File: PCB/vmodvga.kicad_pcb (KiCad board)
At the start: 2 copper layers, 60 parts, among them J1 DE-15, J2 DE-15, J3 VHDCI, U1 ADP3303-3V3, U2 ADP3334, U3 AD9984, U4 ADP3334

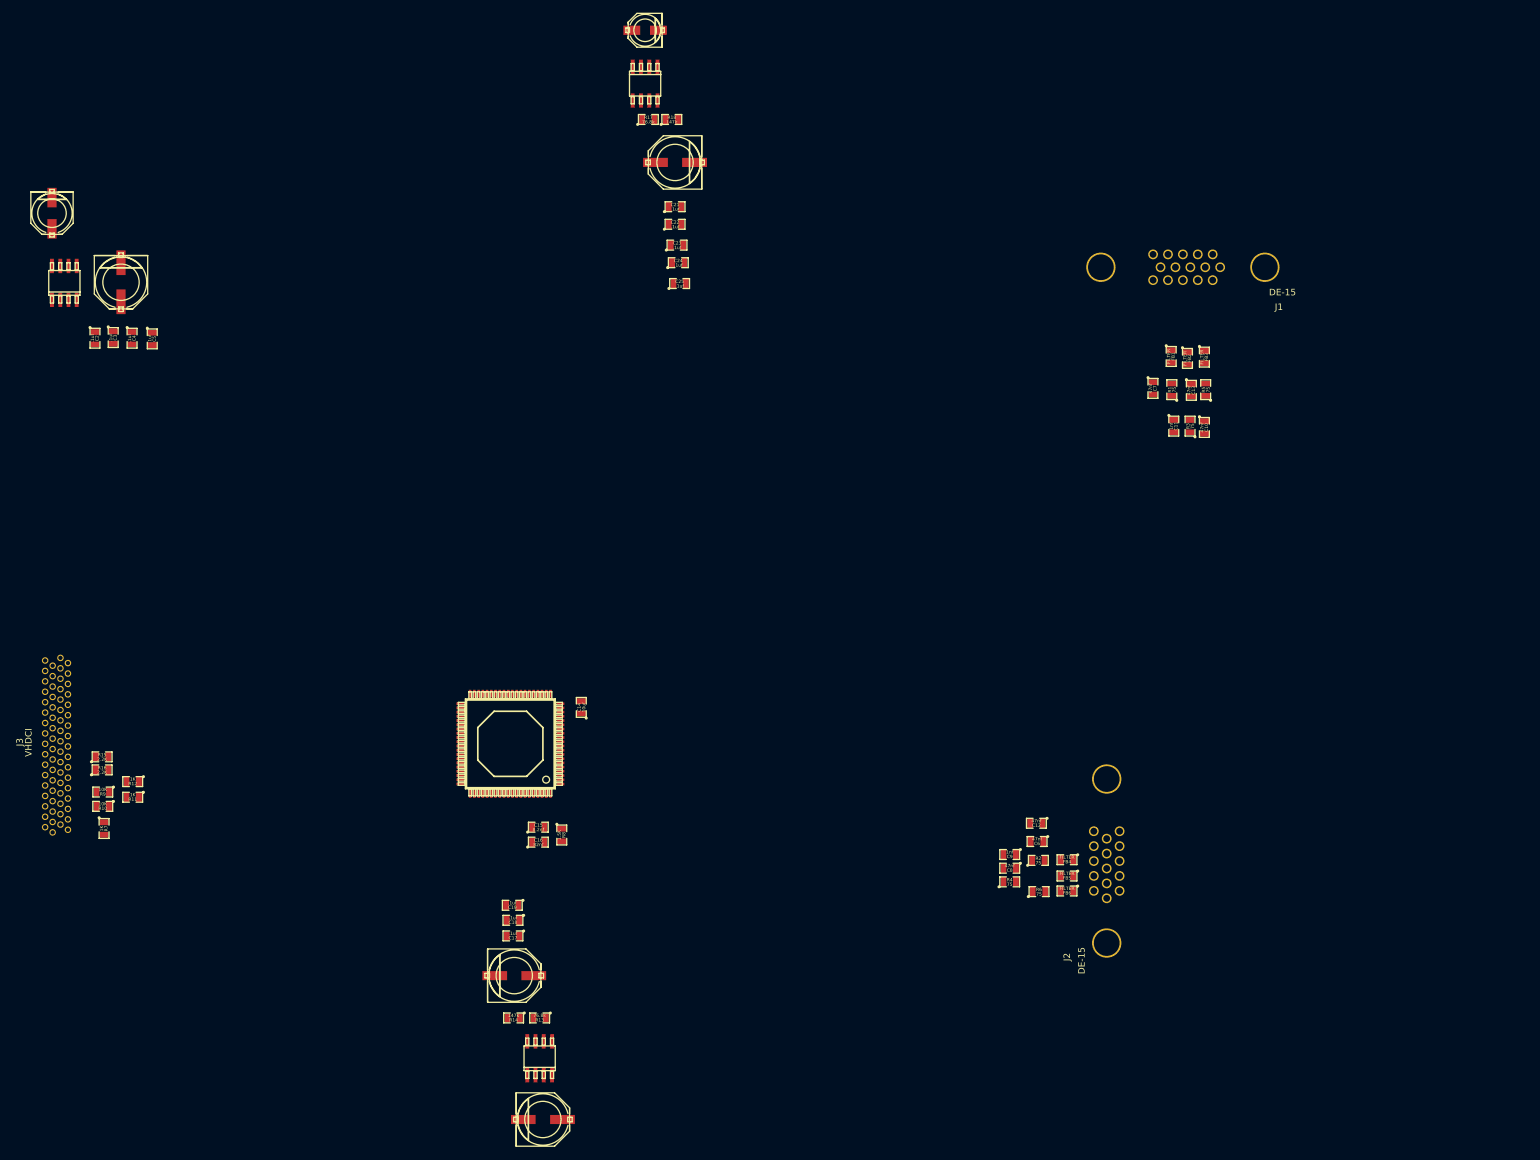
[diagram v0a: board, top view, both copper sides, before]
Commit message: Two VGA connectors without terminal resistors
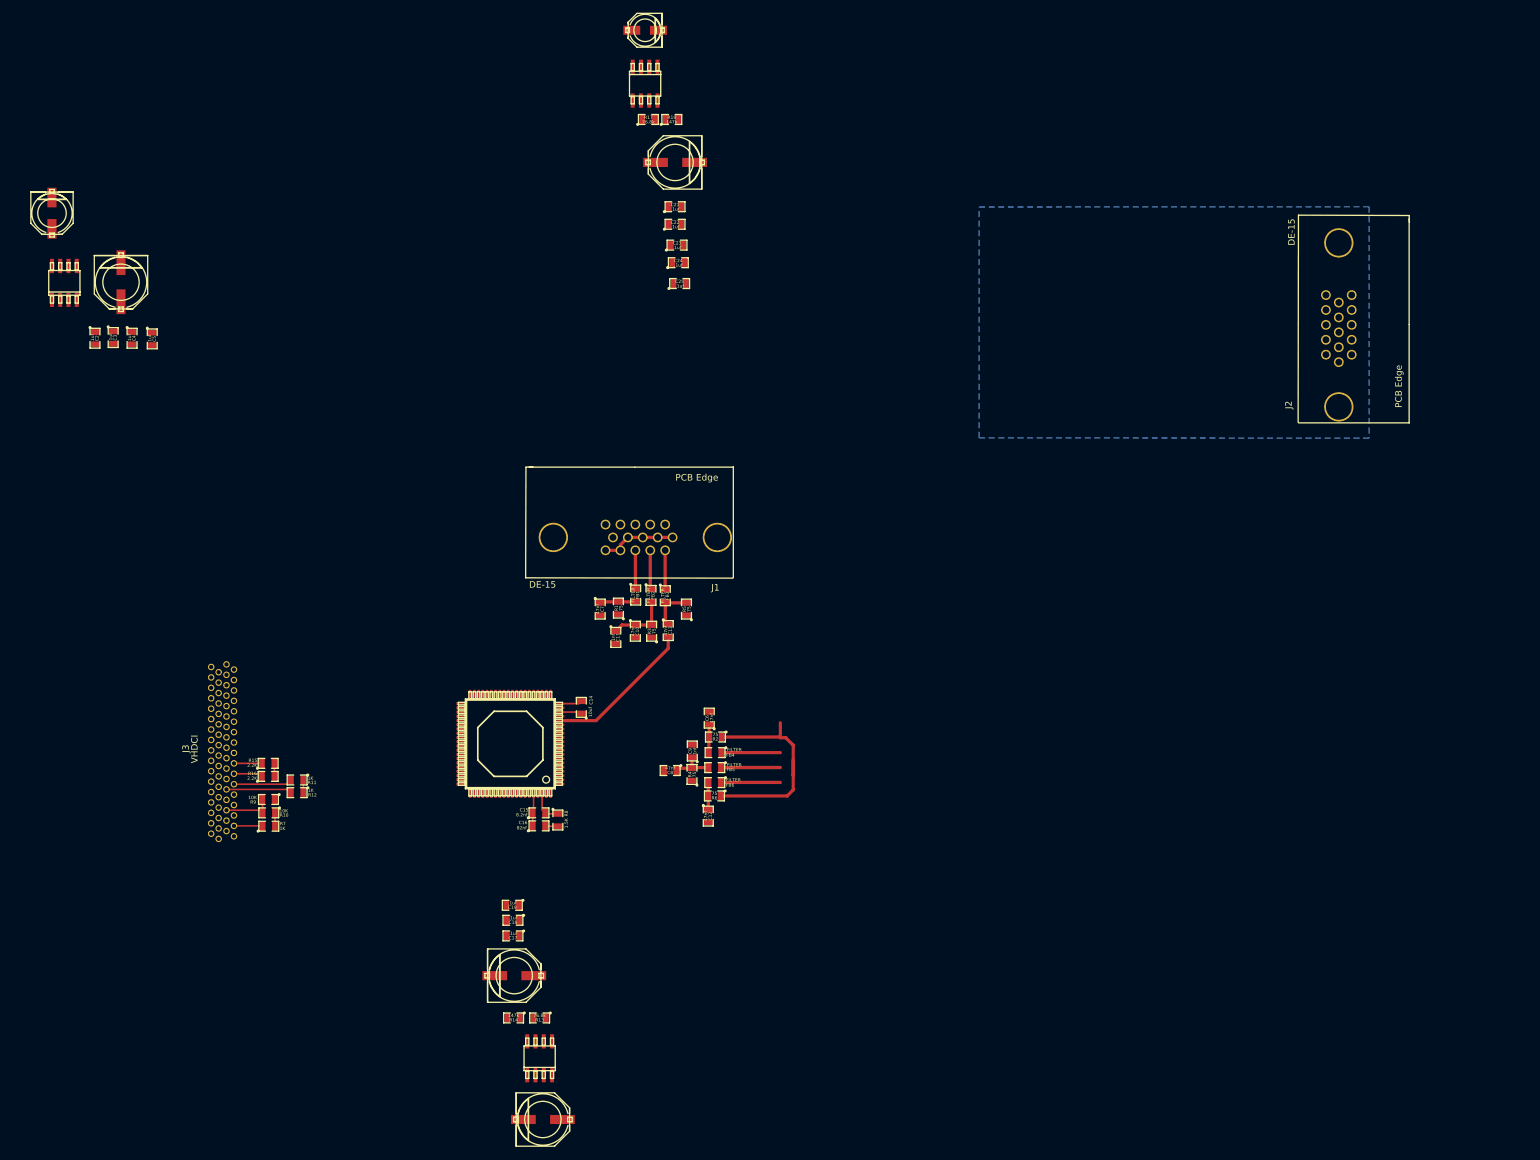
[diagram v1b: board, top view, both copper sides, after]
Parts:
- moved J1 92.9 mm to (140.1, 101.4)
- moved C10 92.8 mm to (140.1, 117.8)
- moved C11 91.6 mm to (137.1, 118.8)
- moved C7 91.4 mm to (134.7, 114.4)
- moved R1 91.4 mm to (137.5, 114.2)
- moved FB3 90.5 mm to (144.7, 112.3)
- moved J2 90.5 mm to (250.2, 70.8)
- moved FB2 90.1 mm to (142.5, 112.3)
- moved FB1 90.0 mm to (140.2, 112.2)
- moved R3 88.5 mm to (142.6, 117.8)
- moved C13 88.4 mm to (145.2, 117.7)
- moved R5 86.6 mm to (147.9, 114.4)
- moved FB5 56.6 mm to (152.3, 138.8)
- moved FB6 56.6 mm to (152.3, 141.1)
- moved FB4 56.5 mm to (152.3, 136.4)
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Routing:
- net /GND: track 0.00 -> 50.1 mm
- net N-0000012: track 0.00 -> 22.9 mm
- net /CLAMP: track 0.00 -> 10.1 mm
- net N-0000014: track 0.00 -> 9.53 mm
- net N-000005: track 0.00 -> 9.13 mm
- net N-000004: track 0.00 -> 9.12 mm
- net N-000003: track 0.00 -> 9.07 mm
- net /COST: track 0.00 -> 9.02 mm
- net /VSOUT: track 0.00 -> 7.91 mm
- net N-0000013: track 0.00 -> 6.94 mm
- net N-0000084: track 0.00 -> 6.85 mm
- net N-0000017: track 0.00 -> 6.03 mm
- net N-0000016: track 0.00 -> 6.01 mm
- net N-0000015: track 0.00 -> 5.94 mm
- net N-000009: track 0.00 -> 5.55 mm
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- added copper zone on B.Cu, net /GND
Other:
- net class Default: clearance 0.254 -> 0.125; trace_width 0.254 -> 0.25; via_dia 0.889 -> 0.45; via_drill 0.635 -> 0.3
- rule trace_clearance: 0.254 -> 0.125
- rule trace_min: 0.254 -> 0.125
- rule via_min_drill: 0.508 -> 0.3
- rule via_min_size: 0.889 -> 0.45

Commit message: Started with PCB design
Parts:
- added P1: 50R, R50x8, F.Cu at (120.3, 66.4)
- added P2: 50R, R50x8, F.Cu at (114.7, 66.6)
- added P3: 50R, R50x8, F.Cu at (108.1, 83.7)
- added P4: 50R, R50x8, F.Cu at (107.3, 77.2)
- added R19: 50, SM0805, F.Cu at (103.5, 82.7)
- added R20: 50, SM0805, F.Cu at (107.1, 81.4)
- added R21: 50, SM0805, F.Cu at (103.5, 80.1)
- added R22: 50, SM0805, F.Cu at (107.0, 78.6)
- moved Cp5 193.1 mm to (252.8, 87.0)
- moved Cp2 181.0 mm to (272.1, 86.1)
- moved C2 175.2 mm to (228.1, 111.2)
- moved U1 171.4 mm to (223.7, 69.0)
- moved C3 170.7 mm to (226.2, 111.2)
- moved R9 166.6 mm to (245.3, 103.0)
- moved C4 166.1 mm to (224.4, 111.2)
- moved R10 163.6 mm to (241.7, 103.0)
- moved Cp1 161.4 mm to (211.2, 69.3)
- moved R15 154.0 mm to (234.4, 106.5)
- moved R12 151.5 mm to (236.2, 110.3)
- moved C5 151.1 mm to (216.2, 88.8)
- moved R16 150.9 mm to (230.8, 106.5)
- moved R14 149.0 mm to (252.7, 106.7)
- moved R13 148.7 mm to (256.3, 106.7)
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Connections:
- J3 pad 1: /B1 -> (no net)
- J3 pad 10: /B7 -> (no net)
- J3 pad 12: /B8 -> (no net)
- J3 pad 13: /B9 -> (no net)
- J3 pad 20: /G0 -> (no net)
- J3 pad 22: /G1 -> (no net)
- J3 pad 23: /G2 -> (no net)
- J3 pad 25: /G3 -> (no net)
- J3 pad 26: /G4 -> (no net)
- J3 pad 28: /G5 -> (no net)
- J3 pad 29: /G6 -> (no net)
- J3 pad 3: /B2 -> (no net)
- J3 pad 31: /G7 -> (no net)
- J3 pad 32: /G8 -> (no net)
- J3 pad 34: /G9 -> (no net)
- J3 pad 35: /B0 -> (no net)
- J3 pad 37: /PWRDWN -> (no net)
- J3 pad 38: /OE_Field -> (no net)
- J3 pad 4: /B3 -> (no net)
- J3 pad 40: /VSOUT -> (no net)
- J3 pad 41: /HSOUT -> (no net)
- J3 pad 43: /SOGOUT -> (no net)
- J3 pad 44: /CLAMP -> (no net)
- J3 pad 45: /COST -> (no net)
- J3 pad 47: /SDA -> (no net)
- J3 pad 49: /SCL -> (no net)
- J3 pad 54: /R0 -> (no net)
- J3 pad 56: /R1 -> (no net)
- J3 pad 57: /R2 -> (no net)
- J3 pad 59: /R3 -> (no net)
- J3 pad 6: /B4 -> (no net)
- J3 pad 60: /R4 -> (no net)
- J3 pad 62: /R5 -> (no net)
- J3 pad 63: /R6 -> (no net)
- J3 pad 65: /R7 -> (no net)
- J3 pad 66: /R8 -> (no net)
- J3 pad 68: /R9 -> (no net)
- J3 pad 7: /B5 -> (no net)
- J3 pad 9: /B6 -> (no net)
- U3 pad 21: /OE_Field -> N-0000092
- U3 pad 22: /VSOUT -> N-0000093
- U3 pad 23: /HSOUT -> N-0000094
- U3 pad 24: /SOGOUT -> N-0000057
- U3 pad 25: /DATACK -> N-0000058
- U3 pad 28: /R9 -> N-0000059
- U3 pad 29: /R8 -> N-0000060
- U3 pad 30: /R7 -> N-0000061
- U3 pad 31: /R6 -> N-0000023
- U3 pad 32: /R5 -> N-0000022
- U3 pad 33: /R4 -> N-0000021
- U3 pad 34: /R3 -> N-0000020
- U3 pad 35: /R2 -> N-0000019
- U3 pad 36: /R1 -> N-0000018
- U3 pad 37: /R0 -> N-0000017
- U3 pad 42: /G9 -> N-0000041
- U3 pad 43: /G8 -> N-0000040
- U3 pad 44: /G7 -> N-0000039
- U3 pad 45: /G6 -> N-0000038
- U3 pad 46: /G5 -> N-0000037
- U3 pad 47: /G4 -> N-0000036
- U3 pad 48: /G3 -> N-0000035
- U3 pad 49: /G2 -> N-0000034
- U3 pad 50: /G1 -> N-0000075
- U3 pad 51: /G0 -> N-0000077
- U3 pad 54: /B9 -> N-0000073
- U3 pad 55: /B8 -> N-0000071
- U3 pad 56: /B7 -> N-0000068
- U3 pad 57: /B6 -> N-0000067
- U3 pad 58: /B5 -> N-0000066
- U3 pad 59: /B4 -> N-0000065
- U3 pad 60: /B3 -> N-0000064
- U3 pad 61: /B2 -> N-0000069
- U3 pad 62: /B1 -> N-0000062
- U3 pad 63: /B0 -> N-0000070
- U3 pad 64: /OVDD -> (no net)
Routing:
- net N-0000082: track 22.9 -> 7.19 mm
- net /CLAMP: track 10.1 -> 0.00 mm
- net /COST: track 9.02 -> 0.00 mm
- net N-0000070: track 0.00 -> 8.16 mm
- net /VSOUT: track 7.91 -> 0.00 mm
- net /GND: track 50.1 -> 58.0 mm
- net N-0000062: track 0.00 -> 7.21 mm
- net N-0000077: track 0.00 -> 7.15 mm
- net N-0000071: track 0.00 -> 7.15 mm
- net N-000007: track 0.00 -> 7.00 mm
- net N-000005: track 0.00 -> 6.98 mm
- net N-0000081: track 0.00 -> 6.77 mm
- net N-0000083: track 0.00 -> 6.75 mm
- net N-0000080: track 0.00 -> 6.57 mm
- net N-000006: track 0.00 -> 6.55 mm
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- added copper zone on F.Cu, net /GND
- removed copper zone on B.Cu, net /GND
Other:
- board outline added: 80 x 60.1 mm

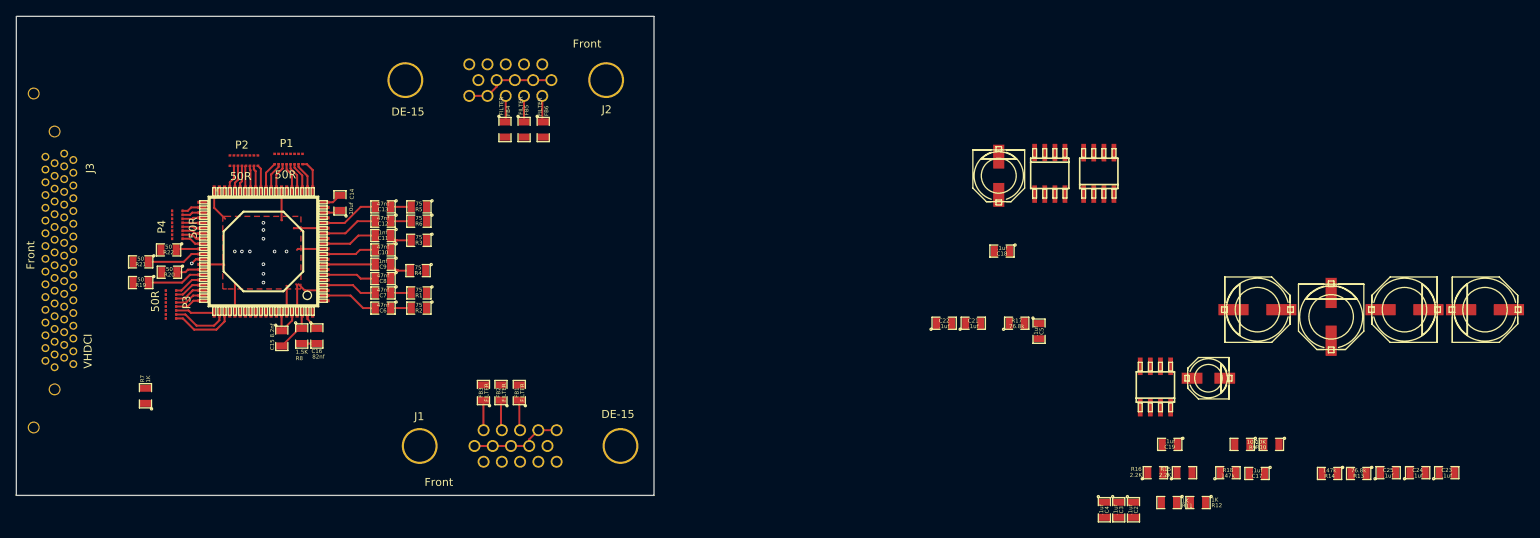
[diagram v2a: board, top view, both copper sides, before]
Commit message: switching to 4 layers
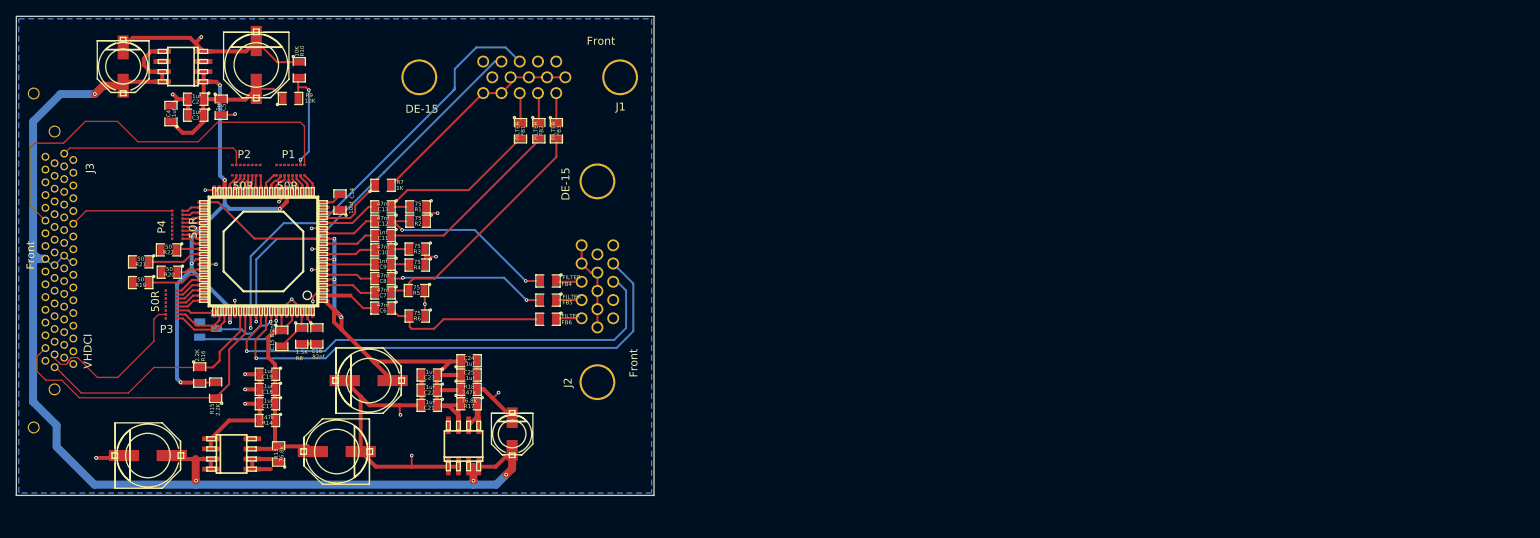
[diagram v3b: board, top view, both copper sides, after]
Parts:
- R11, R12: moved to B.Cu
- moved Cp2 168.7 mm to (104.4, 104.4)
- moved Cp5 138.5 mm to (118.0, 55.4)
- moved R13 135.5 mm to (120.8, 104.2), turned to 90 degrees
- moved R14 133.4 mm to (119.4, 100.0)
- moved R9 130.5 mm to (122.3, 59.6), turned to 0 degrees
- moved Cp6 130.3 mm to (132.1, 95.0), turned to 0 degrees
- moved C2 128.4 mm to (110.4, 59.7), turned to 180 degrees
- moved C23 128.2 mm to (139.7, 94.3), turned to 180 degrees
- moved R10 127.3 mm to (123.4, 56.0), turned to 270 degrees
- moved C4 127.2 mm to (107.3, 61.5), turned to 90 degrees
- moved R12 127.1 mm to (110.9, 88.6), turned to 270 degrees
- moved C3 125.9 mm to (110.4, 61.7), turned to 180 degrees
- moved C17 124.5 mm to (119.4, 97.9)
- moved R15 122.0 mm to (112.9, 96.2), turned to 90 degrees
- moved R11 121.7 mm to (113.0, 87.5), turned to 270 degrees
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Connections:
- C12 pad 1: N-0000014 -> N-0000077
- C13 pad 1: N-0000084 (its old number) -> N-0000075
- C6 pad 1: N-0000012 -> N-0000079
- C7 pad 1: N-0000079 -> N-0000074
- FB1 pad 2: N-0000079 -> N-0000075
- FB3 pad 2: N-0000084 (its old number) -> N-0000074
- FB4 pad 2: N-0000012 -> N-0000077
- FB6 pad 2: N-0000014 -> N-0000079
- J3 pad 1: (no net) -> /R0
- J3 pad 10: (no net) -> /VSOUT
- J3 pad 12: (no net) -> /G9
- J3 pad 13: (no net) -> /G7
- J3 pad 20: (no net) -> /G5
- J3 pad 22: (no net) -> /G3
- J3 pad 23: (no net) -> /G1
- J3 pad 25: (no net) -> /B9
- J3 pad 26: (no net) -> /B7
- J3 pad 28: (no net) -> /B5
- J3 pad 29: (no net) -> /B3
- J3 pad 3: (no net) -> /R2
- J3 pad 31: (no net) -> /B2
- J3 pad 32: (no net) -> /B0
- J3 pad 34: (no net) -> /CLAMP
- J3 pad 35: (no net) -> /R1
- J3 pad 37: (no net) -> /R3
- J3 pad 38: (no net) -> /R5
- J3 pad 4: (no net) -> /R4
- J3 pad 40: (no net) -> /R7
- J3 pad 41: (no net) -> /R9
- J3 pad 43: (no net) -> /HSOUT
- J3 pad 44: (no net) -> /G8
- J3 pad 45: (no net) -> /OE_Field
- J3 pad 47: (no net) -> /G6
- J3 pad 49: (no net) -> /G4
- J3 pad 54: (no net) -> /G2
- J3 pad 56: (no net) -> /G0
- J3 pad 57: (no net) -> /B8
- J3 pad 59: (no net) -> /B6
- J3 pad 6: (no net) -> /R6
- J3 pad 63: (no net) -> /B4
- J3 pad 65: (no net) -> /SCL
- J3 pad 66: (no net) -> /B1
- J3 pad 68: (no net) -> /SDA
- J3 pad 7: (no net) -> /R8
- J3 pad 9: (no net) -> /SOGOUT
- P1 pad 11: (no net) -> /HSOUT
- P1 pad 12: (no net) -> /SOGOUT
- P1 pad 14: (no net) -> /R9
- P1 pad 15: (no net) -> /R8
- P1 pad 16: (no net) -> /R7
- P1 pad 9: (no net) -> /OE_Field
- P2 pad 10: (no net) -> /R5
- P2 pad 11: (no net) -> /R4
- P2 pad 12: (no net) -> /R3
- P2 pad 13: (no net) -> /R2
- P2 pad 14: (no net) -> /R1
- P2 pad 15: (no net) -> /R0
- P2 pad 9: (no net) -> /R6
- P3 pad 1: (no net) -> /B7
- P3 pad 2: (no net) -> /B6
- P3 pad 3: (no net) -> /B5
- P3 pad 4: (no net) -> /B4
- P3 pad 5: (no net) -> /B3
- P3 pad 6: (no net) -> /B2
- P3 pad 7: (no net) -> /B1
- P3 pad 8: (no net) -> /B0
- P4 pad 10: (no net) -> /G8
- P4 pad 11: (no net) -> /G7
- P4 pad 12: (no net) -> /G6
- P4 pad 13: (no net) -> /G5
- P4 pad 14: (no net) -> /G4
- P4 pad 15: (no net) -> /G3
- P4 pad 16: (no net) -> /G2
- P4 pad 9: (no net) -> /G9
- R1 pad 2: N-0000079 -> N-0000075
- R19 pad 2: (no net) -> /B8
- R2 pad 2: N-0000012 -> N-0000077
- R20 pad 2: (no net) -> /B9
- R21 pad 2: (no net) -> /G0
- R22 pad 2: (no net) -> /G1
- R5 pad 2: N-0000084 (its old number) -> N-0000074
- R6 pad 2: N-0000014 -> N-0000079
- U3 pad 64: (no net) -> /OVDD
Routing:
- net /VCC: track 0.00 -> 155.1 mm, vias 0 -> 4
- net /GND: track 58.0 -> 175.7 mm, vias 0 -> 22
- net /OVDD: track 1.52 -> 92.0 mm, vias 1 -> 6
- net /VD: track 0.00 -> 87.9 mm, vias 0 -> 4
- net /VSYNC0: track 0.00 -> 64.6 mm, vias 0 -> 1
- net /HSYNC0: track 0.00 -> 61.2 mm, vias 0 -> 1
- net /HSYNC1: track 0.00 -> 58.0 mm, vias 0 -> 1
- net /OE_Field: track 0.00 -> 52.9 mm
- net /VSYNC1: track 0.00 -> 50.0 mm, vias 0 -> 1
- net /SCL: track 0.00 -> 39.3 mm
- net /SDA: track 0.00 -> 30.8 mm
- net N-0000074: track 0.00 -> 30.8 mm
- net N-0000077: track 0.00 -> 24.4 mm, vias 0 -> 2
- net /PVD: track 7.49 -> 31.7 mm
- net /R0: track 0.00 -> 23.8 mm
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- added copper zone on B.Cu, net /GND
- removed copper zone on F.Cu, net /GND
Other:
- net class Default: trace_width 0.25 -> 0.125
